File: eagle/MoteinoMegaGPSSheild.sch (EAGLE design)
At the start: 24 parts, among them J1 BilgeSwitch, J2 Button, J3 LED, J4 DS18B20, J5 DS18B20, J6 5V_GDN, J7 OKI-78SR-5/1.5, J8 5V, J9 12-24V_VCC, Q1 NDP6020P P-CHANNEL, Q2 IRF9Z14PBF, Q3 2N7000

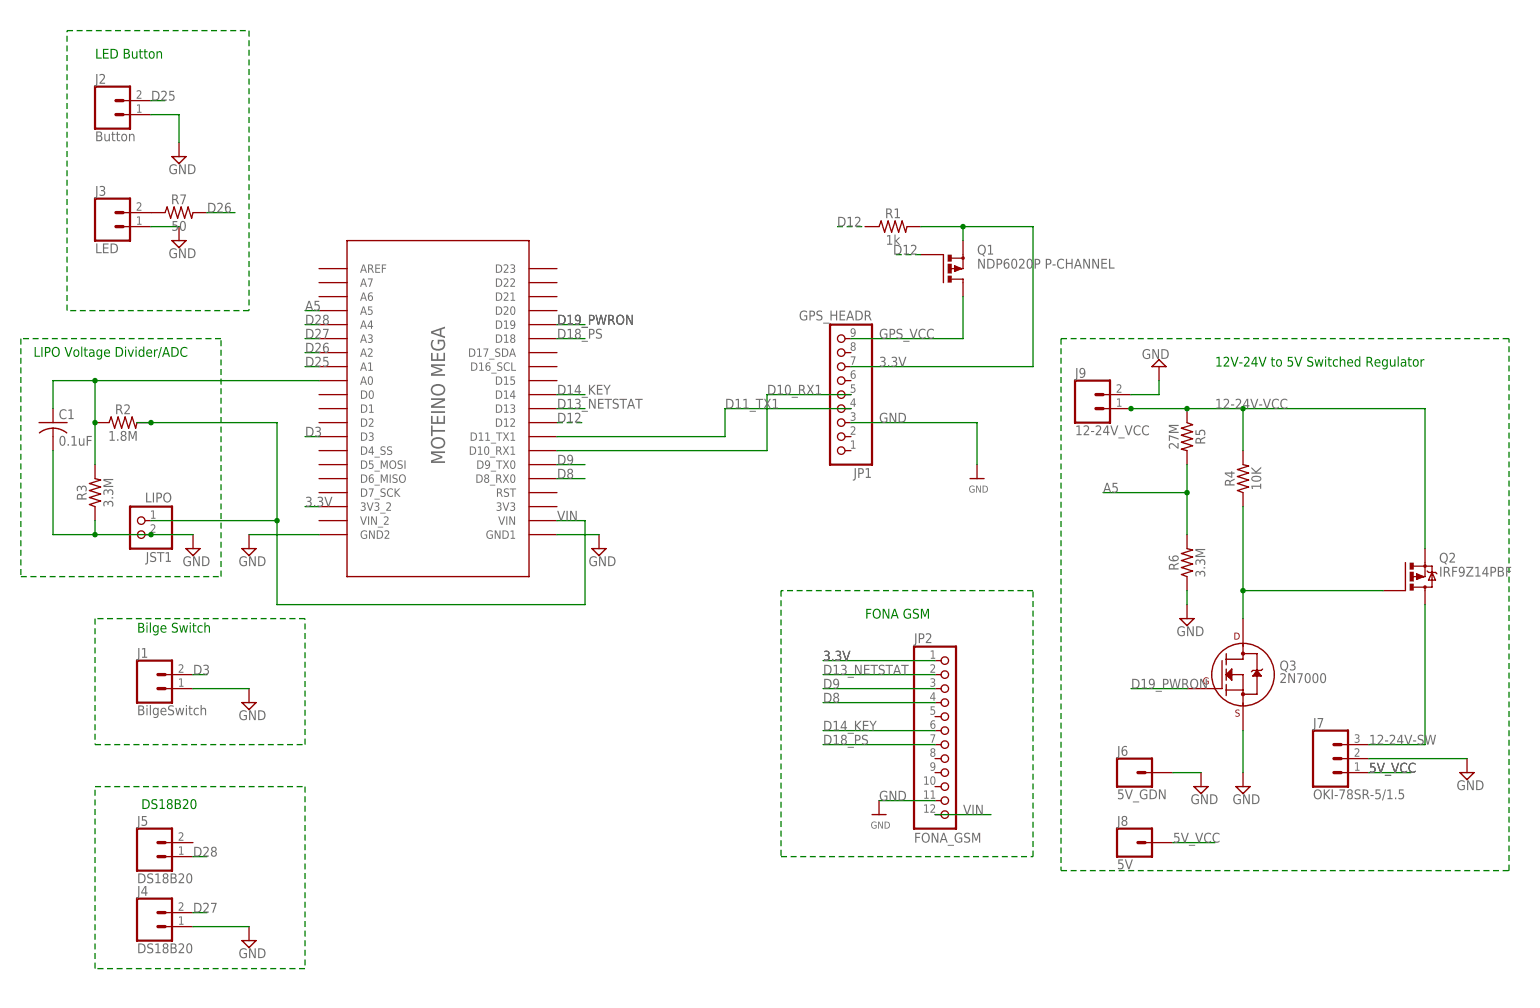
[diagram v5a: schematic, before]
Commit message: V0.91.  Changed netclasses, autorouted, tidied names.  Bar one Width and a few angle errors passes sparkfun and oshpark DRC rules
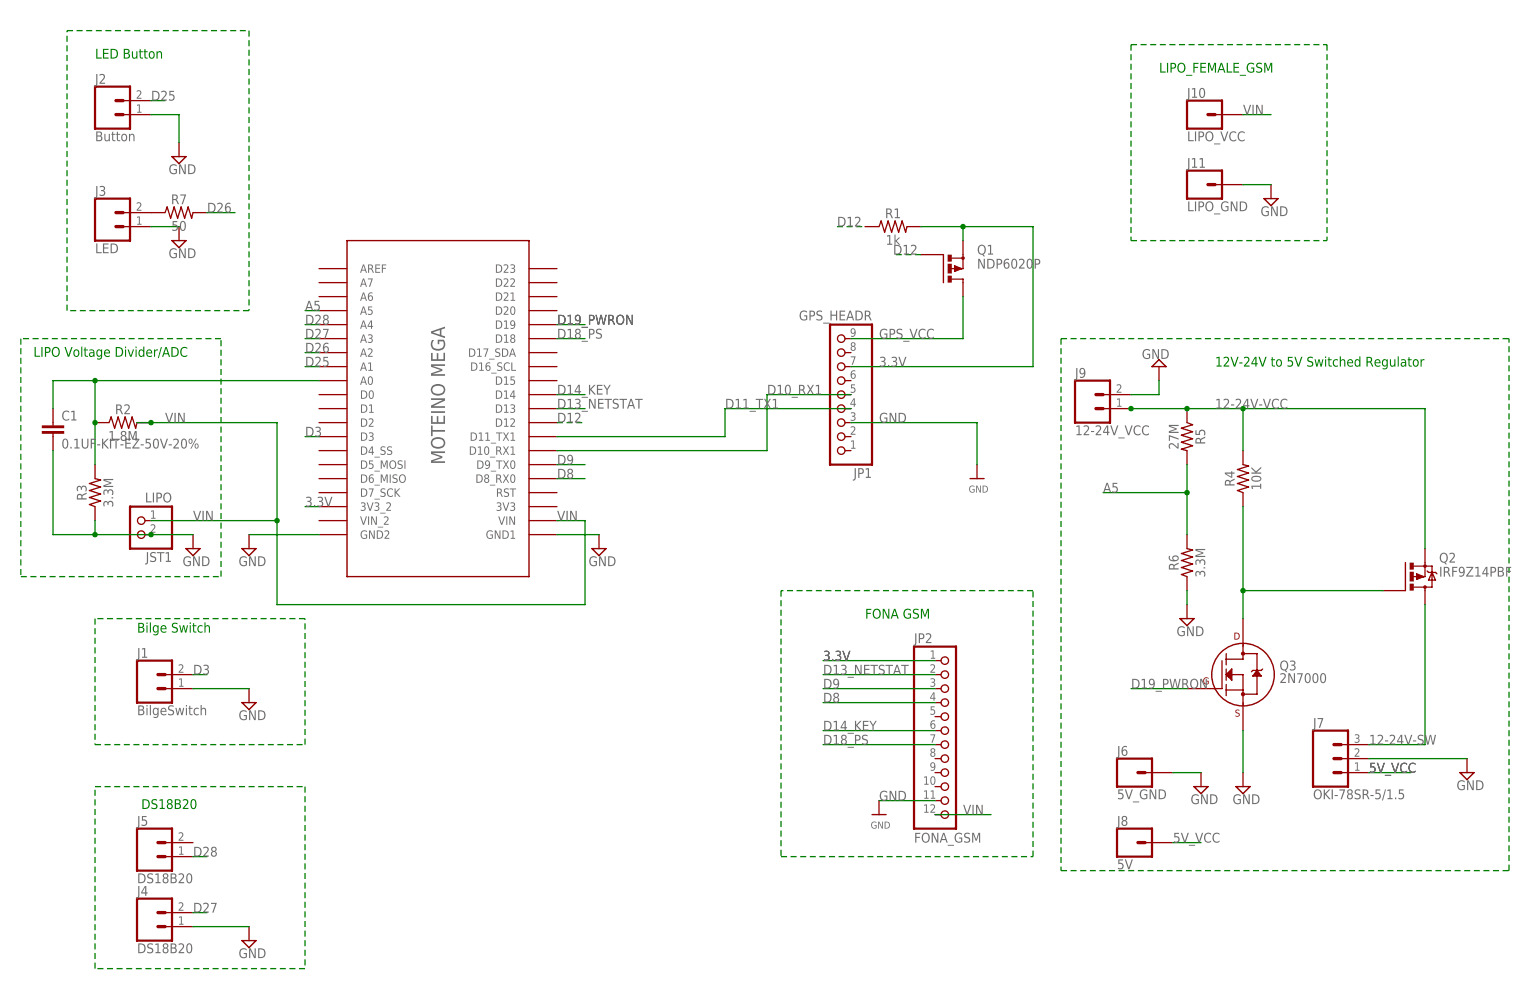
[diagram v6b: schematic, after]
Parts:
- added J10: LIPO_VCC, SparkFun-Connectors:CONN_01
- added J11: LIPO_GND, SparkFun-Connectors:CONN_01
- C1: value 0.1uF -> 0.1UF-KIT-EZ-50V-20%; device adafruit:C-US075-032X103 -> SparkFun-Capacitors:0.1UF-KIT-EZ-50V-20%
- J6: value 5V_GDN -> 5V_GND
- Q1: value NDP6020P P-CHANNEL -> NDP6020P
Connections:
- net GND: now also J11.1
- net VIN: now also J10.1
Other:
- note added: "LIPO_FEMALE_GSM"
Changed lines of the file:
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@@
 <attributes>
 <attribute name="CNAME" value="MoteinoMega ABoatMon Sheild"/>
-<attribute name="CREVISION" value="0.61"/>
+<attribute name="CREVISION" value="0.9"/>
 <attribute name="DESIGNER" value="greg.cope@gmail.com"/>
 </attributes>
@@
 </variantdefs>
 <classes>
-<class number="0" name="default" width="0" drill="0">
+<class number="0" name="default" width="0.254" drill="0">
+<clearance class="0" value="0.254"/>
 </class>
-<class number="1" name="power" width="0.381" drill="0">
+<class number="1" name="power" width="0.6096" drill="0">
 <clearance class="1" value="0.254"/>
 </class>
@@
 <part name="R2" library="SparkFun-Resistors" deviceset="1MOHM" device="-HORIZ_KIT-1/6W-5%" value="1.8M"/>
 <part name="R3" library="SparkFun-Resistors" deviceset="1MOHM" device="-HORIZ_KIT-1/6W-5%" value="3.3M"/>
-<part name="C1" library="adafruit" deviceset="C-US" device="075-032X103" value="0.1uF"/>
-<part name="Q1" library="transistor-power" deviceset="PMOSFET_P" device="TO220BV" value="NDP6020P P-CHANNEL"/>
+<part name="Q1" library="transistor-power" deviceset="PMOSFET_P" device="TO220BV" value="NDP6020P"/>
 <part name="SUPPLY3" library="supply2" deviceset="GND" device=""/>
 <part name="FRAME1" library="SparkFun-Aesthetics" deviceset="FRAME-A4L" device=""/>
@@
 <part name="R6" library="SparkFun-Resistors" deviceset="1MOHM" device="-HORIZ_KIT-1/6W-5%" value="3.3M"/>
 <part name="SUPPLY11" library="supply2" deviceset="GND" device=""/>
-<part name="J6" library="SparkFun-Connectors" deviceset="CONN_01" device="" value="5V_GDN"/>
+<part name="J6" library="SparkFun-Connectors" deviceset="CONN_01" device="" value="5V_GND"/>
 <part name="SUPPLY7" library="supply2" deviceset="GND" device=""/>
 <part name="J9" library="SparkFun-Connectors" deviceset="CONN_02" device="3.5MM-NO_SILK" value="12-24V_VCC"/>
 <part name="SUPPLY12" library="supply2" deviceset="GND" device=""/>
 <part name="R7" library="SparkFun-Resistors" deviceset="1MOHM" device="-HORIZ_KIT-1/6W-5%" value="50"/>
+<part name="C1" library="SparkFun-Capacitors" deviceset="0.1UF" device="-KIT-EZ-50V-20%" value="0.1UF-KIT-EZ-50V-20%"/>
+<part name="J10" library="SparkFun-Connectors" deviceset="CONN_01" device="" value="LIPO_VCC"/>
+<part name="J11" library="SparkFun-Connectors" deviceset="CONN_01" device="" value="LIPO_GND"/>
+<part name="SUPPLY13" library="supply2" deviceset="GND" device=""/>
 </parts>
 <sheets>
@@
 <text x="4.064" y="116.078" size="1.778" layer="91">LIPO Voltage Divider/ADC</text>
 <text x="154.94" y="68.58" size="1.778" layer="91">FONA GSM</text>
+<text x="208.28" y="167.64" size="1.778" layer="91">LIPO_FEMALE_GSM</text>
 </plain>
 <instances>
@@
 <instance part="R2" gate="G$1" x="20.32" y="104.14"/>
 <instance part="R3" gate="G$1" x="15.24" y="91.44" rot="R90"/>
-<instance part="C1" gate="G$1" x="7.62" y="104.14"/>
 <instance part="Q1" gate="G$1" x="170.18" y="132.08"/>
 <instance part="SUPPLY3" gate="GND" x="43.18" y="53.34"/>
@@
 <instance part="SUPPLY12" gate="GND" x="208.28" y="114.3" rot="R180"/>
 <instance part="R7" gate="G$1" x="30.48" y="142.24"/>
+<instance part="C1" gate="G$1" x="7.62" y="101.6"/>
+<instance part="J10" gate="G$1" x="215.9" y="160.02"/>
+<instance part="J11" gate="G$1" x="215.9" y="147.32"/>
+<instance part="SUPPLY13" gate="GND" x="228.6" y="144.78"/>
 </instances>
 <busses>
 </busses>
 <nets>
-<net name="GND" class="0">
+<net name="GND" class="1">
 <segment>
 <wire x1="175.26" y1="104.14" x2="175.26" y2="96.52" width="0.1524" layer="91"/>
@@
 <wire x1="15.24" y1="86.36" x2="15.24" y2="83.82" width="0.1524" layer="91"/>
 <wire x1="15.24" y1="83.82" x2="7.62" y2="83.82" width="0.1524" layer="91"/>
-<pinref part="C1" gate="G$1" pin="2"/>
 <wire x1="7.62" y1="83.82" x2="7.62" y2="99.06" width="0.1524" layer="91"/>
 <wire x1="15.24" y1="83.82" x2="25.4" y2="83.82" width="0.1524" layer="91"/>
 <junction x="15.24" y="83.82"/>
 <junction x="25.4" y="83.82"/>
+<pinref part="C1" gate="G$1" pin="2"/>
 </segment>
 <segment>
@@
 <wire x1="208.28" y1="109.22" x2="208.28" y2="111.76" width="0.1524" layer="91"/>
 <pinref part="SUPPLY12" gate="GND" pin="GND"/>
+</segment>
+<segment>
+<pinref part="J11" gate="G$1" pin="1"/>
+<wire x1="223.52" y1="147.32" x2="228.6" y2="147.32" width="0.1524" layer="91"/>
+<pinref part="SUPPLY13" gate="GND" pin="GND"/>
 </segment>
 </net>
@@
 <junction x="48.26" y="86.36"/>
 <label x="99.06" y="86.36" size="1.778" layer="95"/>
+<label x="33.02" y="86.36" size="1.778" layer="95"/>
+<label x="27.94" y="104.14" size="1.778" layer="95"/>
 </segment>
 <segment>
@@
 <label x="172.72" y="33.02" size="1.778" layer="95"/>
 </segment>
+<segment>
+<pinref part="J10" gate="G$1" pin="1"/>
+<wire x1="223.52" y1="160.02" x2="228.6" y2="160.02" width="0.1524" layer="91"/>
+<label x="223.52" y="160.02" size="1.778" layer="95"/>
+</segment>
 </net>
 <net name="A0" class="0">
 <segment>
 <pinref part="R3" gate="G$1" pin="2"/>
-<pinref part="C1" gate="G$1" pin="1"/>
 <wire x1="15.24" y1="96.52" x2="15.24" y2="104.14" width="0.1524" layer="91"/>
 <wire x1="15.24" y1="104.14" x2="15.24" y2="111.76" width="0.1524" layer="91"/>
@@
 <wire x1="15.24" y1="111.76" x2="55.88" y2="111.76" width="0.1524" layer="91"/>
 <junction x="15.24" y="111.76"/>
+<pinref part="C1" gate="G$1" pin="1"/>
 </segment>
 </net>
@@
 </segment>
 </net>
-<net name="3.3V" class="0">
+<net name="3.3V" class="1">
 <segment>
 <wire x1="185.42" y1="114.3" x2="185.42" y2="139.7" width="0.1524" layer="91"/>
@@
 </segment>
 </net>
-<net name="12-24V-VCC" class="0">
+<net name="12-24V-VCC" class="1">
 <segment>
 <pinref part="R4" gate="G$1" pin="2"/>
@@
 <wire x1="271.78" y1="22.86" x2="271.78" y2="119.38" width="0.1524" layer="91" style="longdash"/>
 </segment>
-</net>
-<net name="GPS_VCC" class="0">
+<segment>
+<wire x1="203.2" y1="172.72" x2="238.76" y2="172.72" width="0.1524" layer="91" style="longdash"/>
+</segment>
+<segment>
+<wire x1="203.2" y1="172.72" x2="203.2" y2="137.16" width="0.1524" layer="91" style="longdash"/>
+</segment>
+<segment>
+<wire x1="238.76" y1="172.72" x2="238.76" y2="137.16" width="0.1524" layer="91" style="longdash"/>
+</segment>
+<segment>
+<wire x1="203.2" y1="137.16" x2="238.76" y2="137.16" width="0.1524" layer="91" style="longdash"/>
+</segment>
+</net>
+<net name="GPS_VCC" class="1">
 <segment>
 <pinref part="JP1" gate="A" pin="9"/>
@@
 </segment>
 </net>
-<net name="N$2" class="0">
+<net name="N$2" class="1">
 <segment>
 <pinref part="Q3" gate="G$1" pin="D"/>
@@
 </segment>
 </net>
-<net name="12-24V-SW" class="0">
+<net name="12-24V-SW" class="1">
 <segment>
 <pinref part="Q2" gate="G$1" pin="D"/>
@@
 </segment>
 </net>
-<net name="5V_VCC" class="0">
+<net name="5V_VCC" class="1">
 <segment>
 <pinref part="J7" gate="J$1" pin="1"/>
@@
 <segment>
 <pinref part="J8" gate="G$1" pin="1"/>
-<wire x1="210.82" y1="27.94" x2="218.44" y2="27.94" width="0.1524" layer="91"/>
+<wire x1="210.82" y1="27.94" x2="215.9" y2="27.94" width="0.1524" layer="91"/>
 <label x="210.82" y="27.94" size="1.778" layer="95"/>
 </segment>

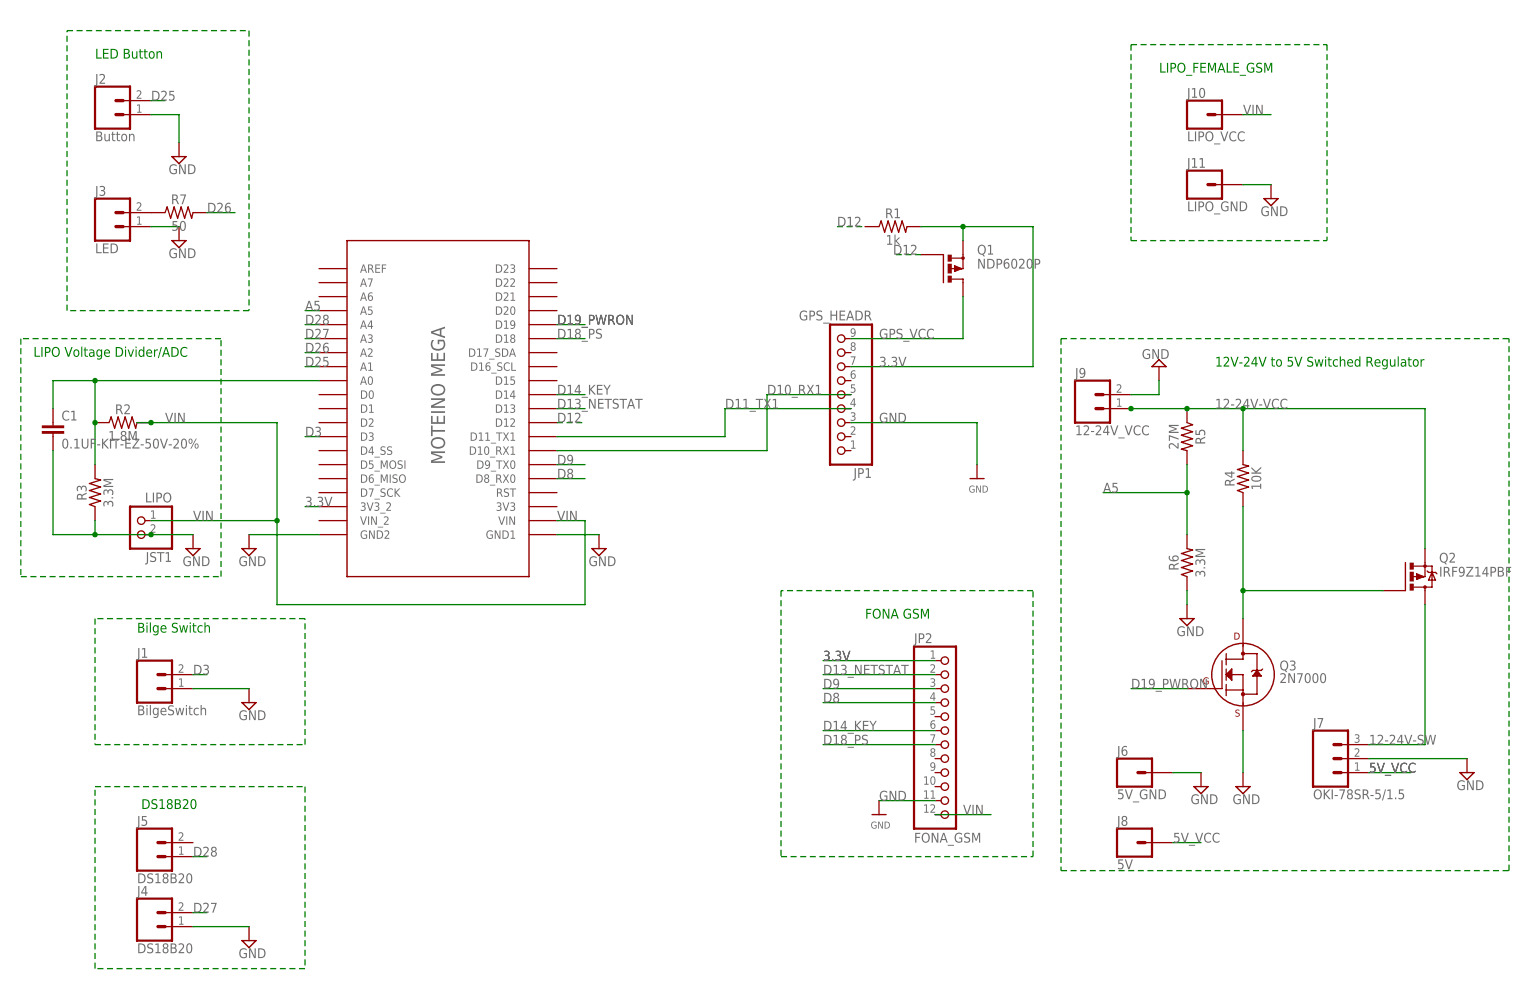
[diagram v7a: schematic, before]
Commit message: V0.98, schematic layout tweaks, corrected GSM power error, removed GSM power
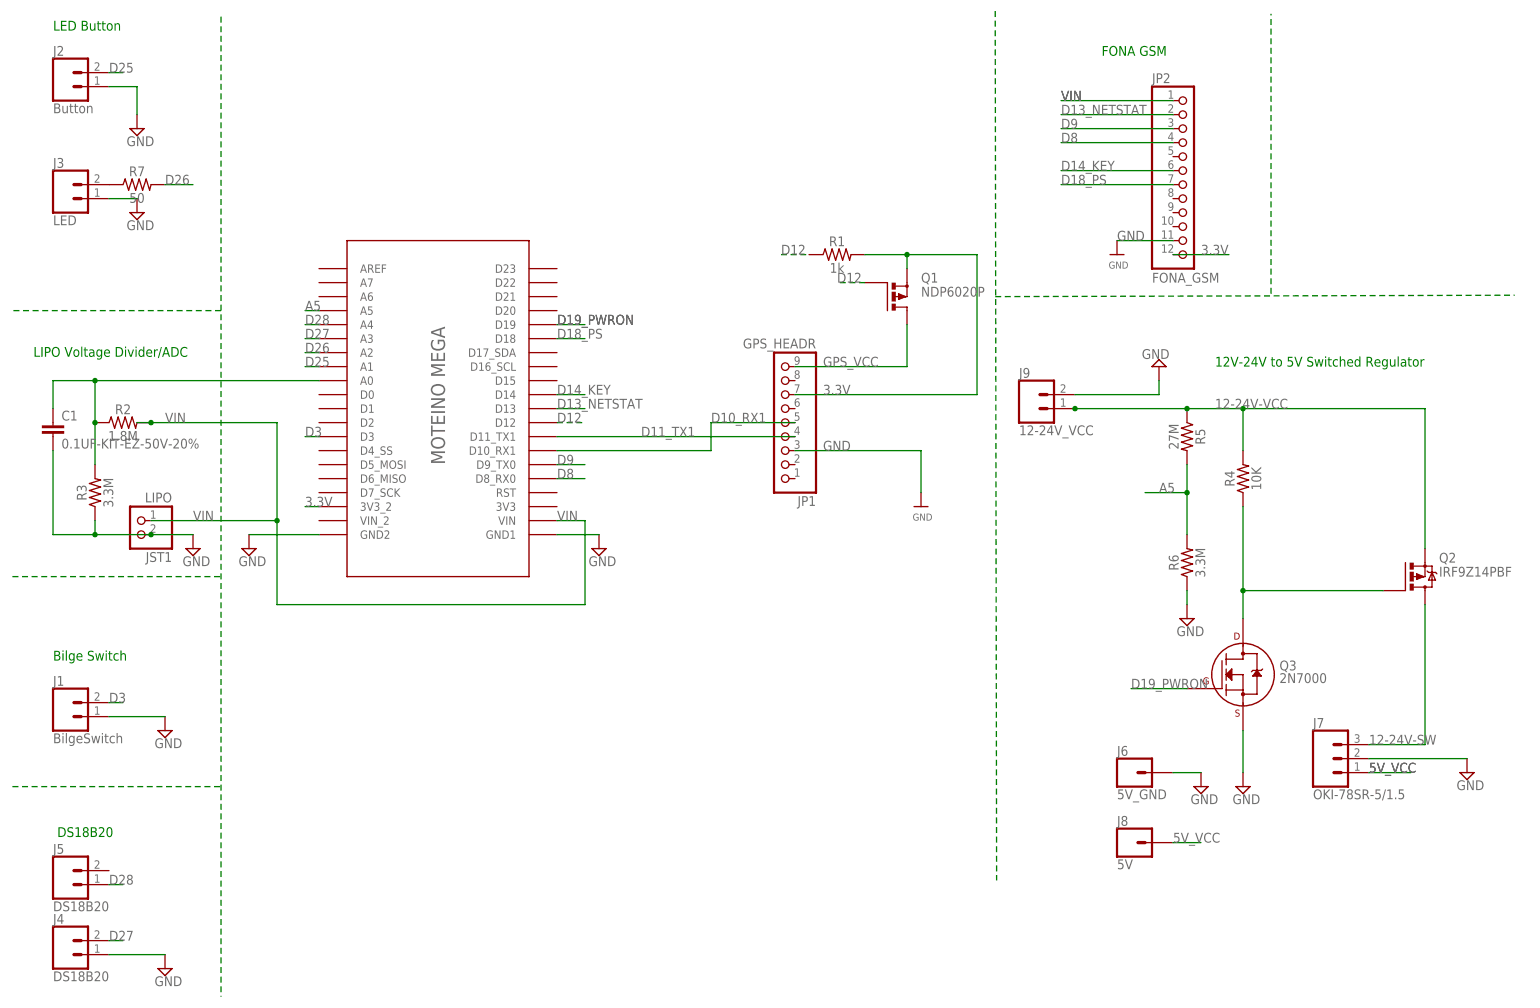
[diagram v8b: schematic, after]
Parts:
- removed J10: LIPO_VCC, SparkFun-Connectors:CONN_01
- removed J11: LIPO_GND, SparkFun-Connectors:CONN_01
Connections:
- net 3.3V: now also JP2.12; no longer JP2.1
- net GND: no longer J11.1
- net VIN: now also JP2.1; no longer J10.1, JP2.12
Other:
- note removed: "LIPO_FEMALE_GSM"
- moved on the sheet: J1, J2, J3, J4, J5, J9, JP1, JP2, Q1, R1, R7
